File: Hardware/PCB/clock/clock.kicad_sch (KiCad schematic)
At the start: 63 parts, among them J2 Synth_power_2x5, J3 AudioJack2, J4 AudioJack2, J5 AudioJack2, J6 AudioJack2, J7 AudioJack2, J8 Conn_02x04_Odd_Even, J9 Conn_02x04_Odd_Even, SW1 RotaryEncoder, SW2 SW_Push, U1 40106

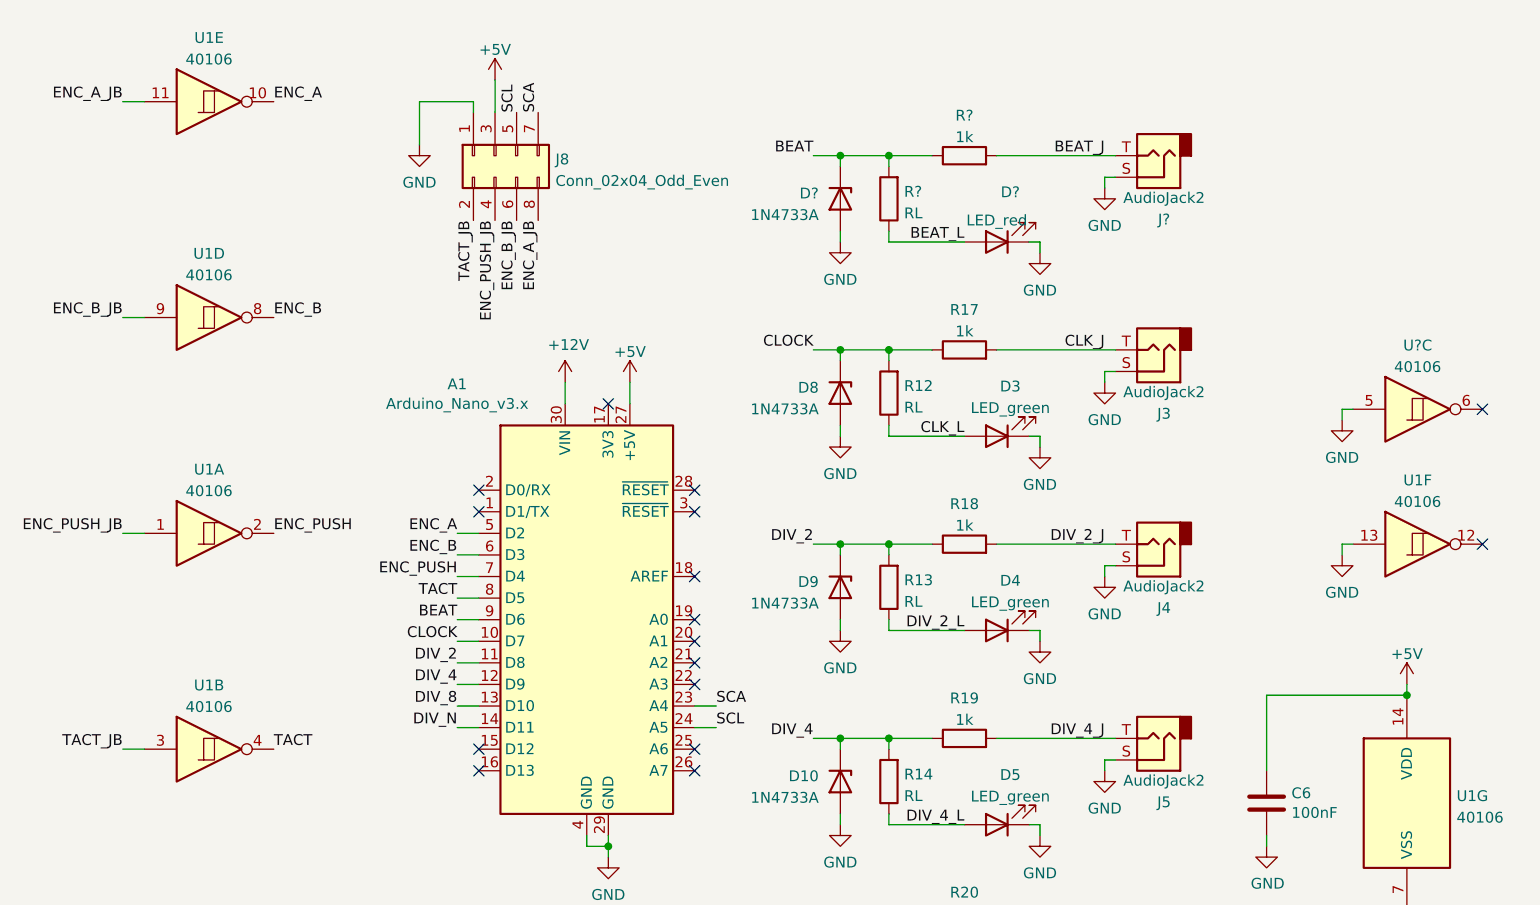
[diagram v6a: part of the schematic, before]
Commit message: Reset counts when changing division; update schematic and layout with beat output, no ext clock, and unimpeded Nano USB
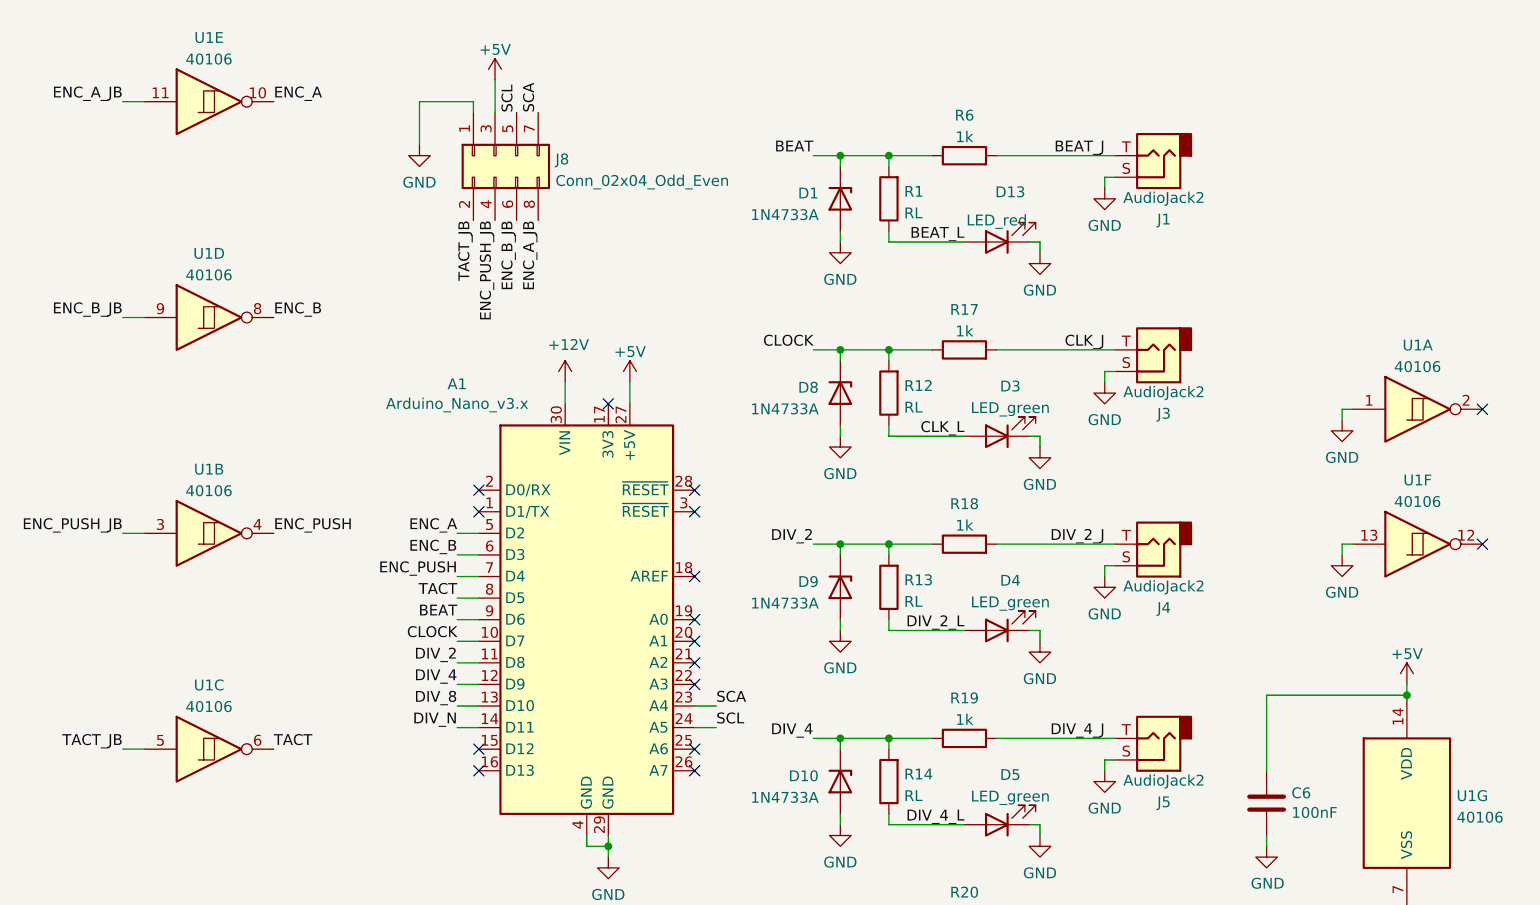
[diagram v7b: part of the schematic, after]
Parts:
- A1: footprint Module:Arduino_Nano -> ao_tht:Arduino_Nano
- gave numbers to parts that had none: 6
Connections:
- net ENC_PUSH: now also U1.4; no longer U1.2
- net ENC_PUSH_JB: now also U1.3; no longer U1.1
- net GND: now also U1.1; no longer U1.5
- net TACT: now also U1.6; no longer U1.4
- net TACT_JB: now also U1.5; no longer U1.3
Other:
- moved on the sheet: U1A, U1B, U1C

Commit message: PCB adjustments
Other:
- note added: "With BOM LEDs I chose RL = 2k for red, RL = 470R for green"
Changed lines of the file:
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@@
     )
+  )
+  (text "With BOM LEDs I chose\nRL = 2k for red, RL = \n470R for green"
+    (at 233.68 40.005 0)
+    (effects (font (size 1.27 1.27)) (justify left bottom))
   )
   (label "ENC_A" (at 139.7 76.2 180)
